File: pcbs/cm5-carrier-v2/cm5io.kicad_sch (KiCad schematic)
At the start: 27 parts, among them J801 48406-0003, J802 ARJM11D7-502-AB-EW2, J803 TYPE-C-31-M-12, J804 FH12-20S-0.5SH, J805 FH12-20S-0.5SH, J806 FFC3A20-05-G, U801 PESD4USB3BTTS-QX, U802 PESD4USB3BTTS-QX, U803 PESD4USB3BTTS-QX, U804 PESD4USB3BTTS-QX, U805 PESD4USB3BTTS-QX, U806 AP22653FDZ-7, U807 PESD4USB3BTTS-QX, U808 PESD4USB3BTTS-QX

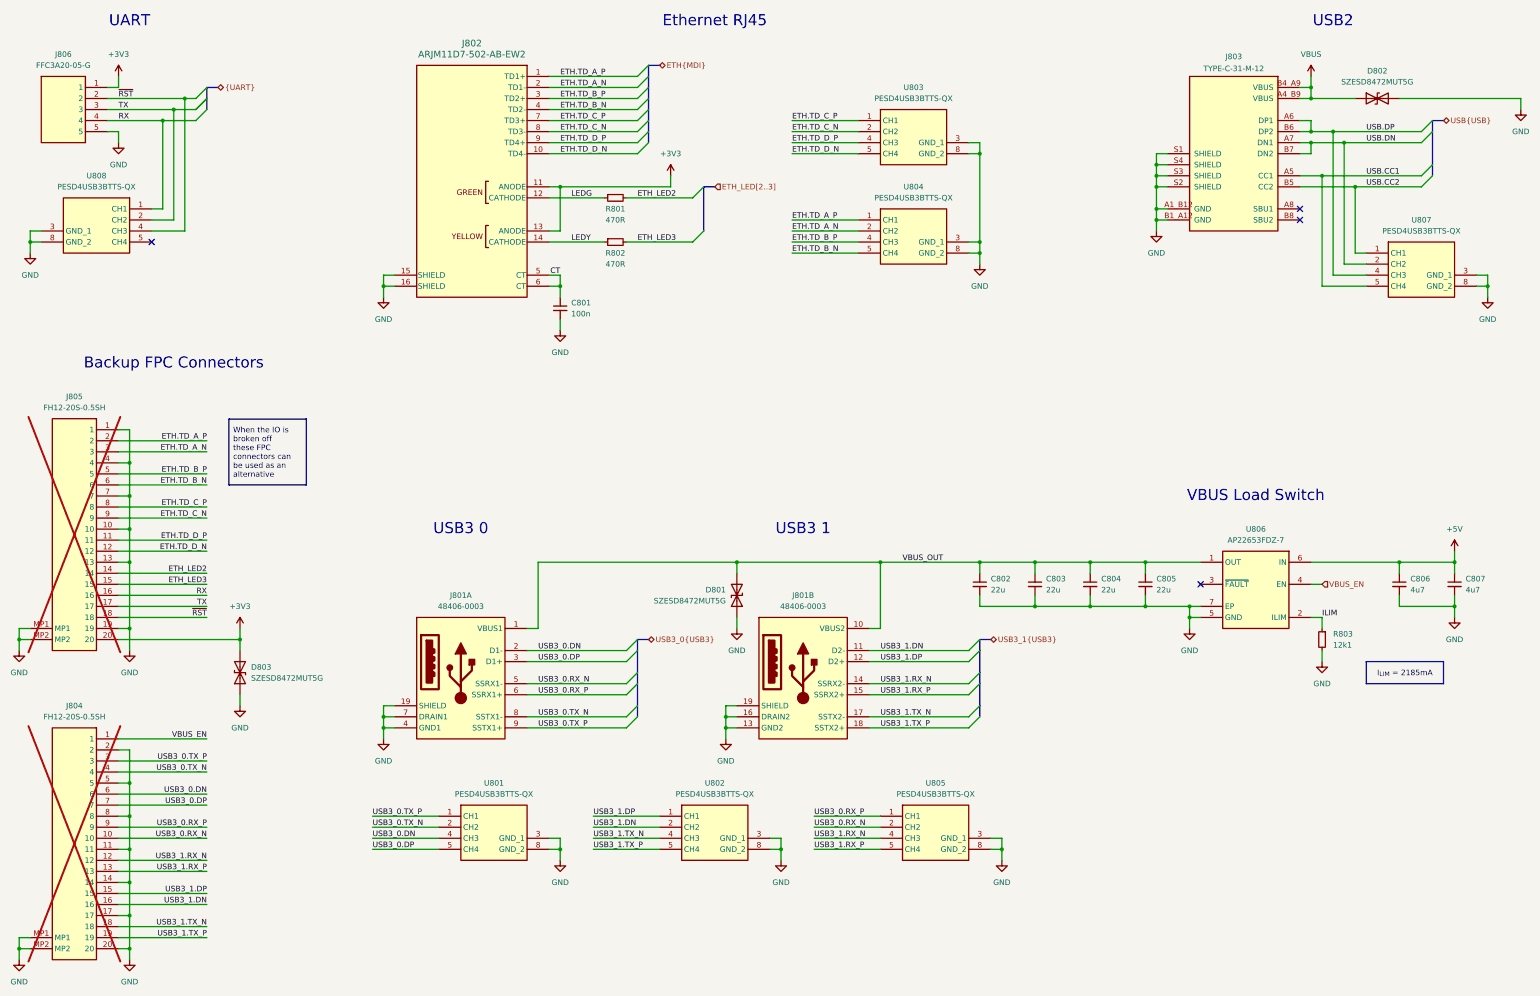
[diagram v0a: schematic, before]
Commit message: Changed UART connector to I2C
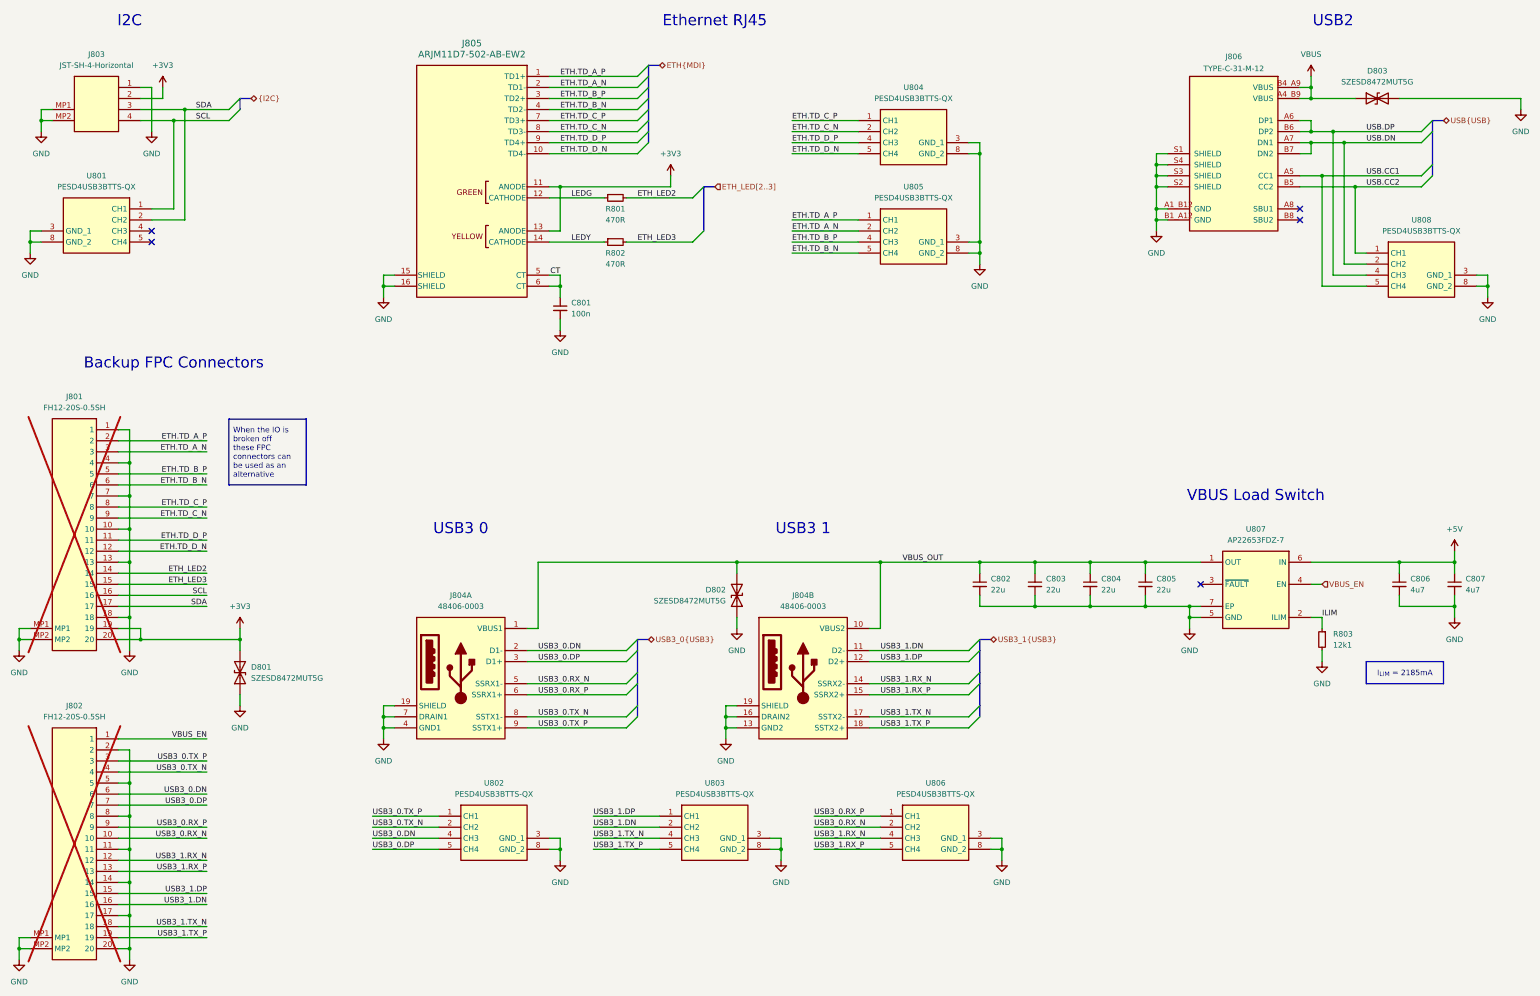
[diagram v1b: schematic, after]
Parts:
- removed J806: FFC3A20-05-G, project_footprints:FFC3A2005G, symbol CONN-FPC:FFC3A20-05-G
- added J803: JST-SH-4-Horizontal, project_footprints:JST_SH_SM04B-SRSS-TB_1x04-1MP_P1.00mm_Horizontal, symbol JST:JST-SH-4-Horizontal
- renumbered D803 to D801, D801 to D802, D802 to D803, J805 to J801, J804 to J802, J801 to J804, J802 to J805, J803 to J806, U808 to U801, U801 to U802, U802 to U803, U803 to U804, U804 to U805, U805 to U806, U806 to U807, U807 to U808
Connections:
- net +3V3: now also J801.19, J803.2
- net GND: now also J801.18, J803.1, J803.MP1, J803.MP2; no longer J801.19
- net RX renamed SCL
- net SCL: now also J803.4
- net TX renamed SDA
- net SDA: now also J803.3
- net ~{RST}: no longer names the net of U801.4 (CH3), U801.7 (NC)
- net ~{RST}: no longer J801.18
- no-connect marks 4 -> 5
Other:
- note added: "I2C"
- note removed: "UART"
